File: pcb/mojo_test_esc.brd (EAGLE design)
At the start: 100 x 80 mm, 0 parts

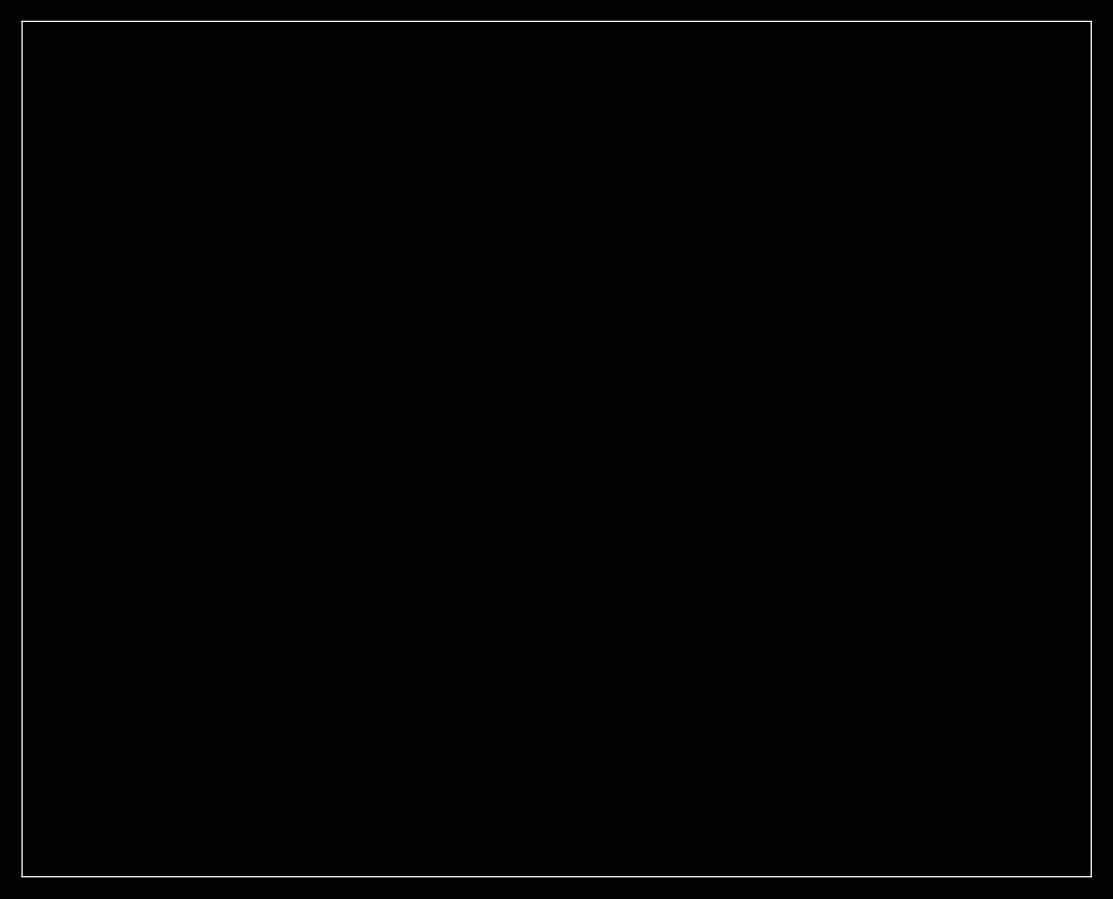
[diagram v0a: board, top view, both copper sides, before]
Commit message: Creating basic board layout/schematic from Mojo pinout
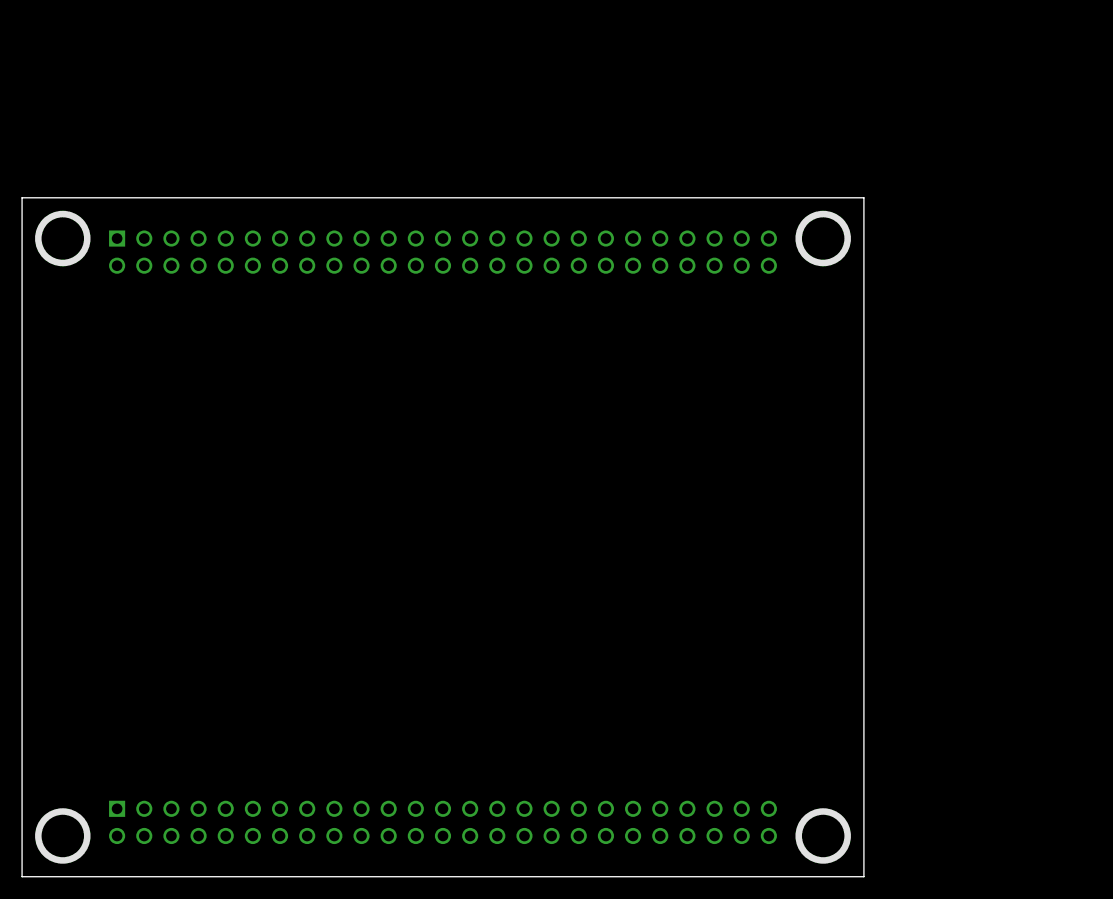
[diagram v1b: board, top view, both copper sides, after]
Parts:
- added B1: MOJO_NO_ANALOGV3_NO_LABEL, mojo_test_esc:MOJO_V3_NO_LABEL_NO_ANALOG
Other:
- board size 100 x 80 mm -> 78.7 x 63.5 mm
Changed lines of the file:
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@@
 <layer number="48" name="Document" color="7" fill="1" visible="yes" active="yes"/>
 <layer number="49" name="Reference" color="7" fill="1" visible="yes" active="yes"/>
+<layer number="50" name="dxf" color="7" fill="1" visible="no" active="no"/>
 <layer number="51" name="tDocu" color="7" fill="1" visible="yes" active="yes"/>
 <layer number="52" name="bDocu" color="7" fill="1" visible="yes" active="yes"/>
+<layer number="53" name="tGND_GNDA" color="7" fill="9" visible="no" active="no"/>
+<layer number="54" name="bGND_GNDA" color="1" fill="9" visible="no" active="no"/>
+<layer number="56" name="wert" color="7" fill="1" visible="no" active="no"/>
+<layer number="57" name="tCAD" color="7" fill="1" visible="no" active="no"/>
+<layer number="59" name="tCarbon" color="7" fill="1" visible="no" active="no"/>
+<layer number="60" name="bCarbon" color="7" fill="1" visible="no" active="no"/>
 <layer number="90" name="Modules" color="5" fill="1" visible="no" active="no"/>
 <layer number="91" name="Nets" color="2" fill="1" visible="no" active="no"/>
@@
 <layer number="97" name="Info" color="7" fill="1" visible="no" active="no"/>
 <layer number="98" name="Guide" color="6" fill="1" visible="no" active="no"/>
+<layer number="99" name="SpiceOrder" color="7" fill="1" visible="no" active="no"/>
+<layer number="100" name="Muster" color="7" fill="1" visible="no" active="no"/>
+<layer number="101" name="Patch_Top" color="12" fill="4" visible="yes" active="yes"/>
+<layer number="102" name="Vscore" color="7" fill="1" visible="yes" active="yes"/>
+<layer number="103" name="tMap" color="7" fill="1" visible="yes" active="yes"/>
+<layer number="104" name="Name" color="16" fill="1" visible="yes" active="yes"/>
+<layer number="105" name="tPlate" color="7" fill="1" visible="yes" active="yes"/>
+<layer number="106" name="bPlate" color="7" fill="1" visible="yes" active="yes"/>
+<layer number="107" name="Crop" color="7" fill="1" visible="yes" active="yes"/>
+<layer number="108" name="tplace-old" color="10" fill="1" visible="yes" active="yes"/>
+<layer number="109" name="ref-old" color="11" fill="1" visible="yes" active="yes"/>
+<layer number="110" name="fp0" color="7" fill="1" visible="yes" active="yes"/>
+<layer number="111" name="LPC17xx" color="7" fill="1" visible="yes" active="yes"/>
+<layer number="112" name="tSilk" color="7" fill="1" visible="yes" active="yes"/>
+<layer number="113" name="IDFDebug" color="7" fill="1" visible="yes" active="yes"/>
+<layer number="114" name="Badge_Outline" color="11" fill="1" visible="no" active="no"/>
+<layer number="115" name="ReferenceISLANDS" color="7" fill="1" visible="yes" active="yes"/>
+<layer number="116" name="Patch_BOT" color="9" fill="4" visible="yes" active="yes"/>
+<layer number="118" name="Rect_Pads" color="7" fill="1" visible="yes" active="yes"/>
+<layer number="121" name="_tsilk" color="7" fill="1" visible="yes" active="yes"/>
+<layer number="122" name="_bsilk" color="7" fill="1" visible="yes" active="yes"/>
+<layer number="123" name="tTestmark" color="7" fill="1" visible="yes" active="yes"/>
+<layer number="124" name="bTestmark" color="7" fill="1" visible="yes" active="yes"/>
+<layer number="125" name="_tNames" color="7" fill="1" visible="yes" active="yes"/>
+<layer number="126" name="_bNames" color="7" fill="1" visible="yes" active="yes"/>
+<layer number="127" name="_tValues" color="7" fill="1" visible="yes" active="yes"/>
+<layer number="128" name="_bValues" color="7" fill="1" visible="yes" active="yes"/>
+<layer number="129" name="Mask" color="7" fill="1" visible="yes" active="yes"/>
+<layer number="131" name="tAdjust" color="7" fill="1" visible="yes" active="yes"/>
+<layer number="132" name="bAdjust" color="7" fill="1" visible="yes" active="yes"/>
+<layer number="144" name="Drill_legend" color="7" fill="1" visible="yes" active="yes"/>
+<layer number="150" name="Notes" color="7" fill="1" visible="yes" active="yes"/>
+<layer number="151" name="HeatSink" color="7" fill="1" visible="yes" active="yes"/>
+<layer number="152" name="_bDocu" color="7" fill="1" visible="yes" active="yes"/>
+<layer number="153" name="FabDoc1" color="7" fill="1" visible="yes" active="yes"/>
+<layer number="154" name="FabDoc2" color="7" fill="1" visible="yes" active="yes"/>
+<layer number="155" name="FabDoc3" color="7" fill="1" visible="yes" active="yes"/>
+<layer number="199" name="Contour" color="7" fill="1" visible="yes" active="yes"/>
+<layer number="200" name="200bmp" color="1" fill="10" visible="yes" active="yes"/>
+<layer number="201" name="201bmp" color="2" fill="10" visible="yes" active="yes"/>
+<layer number="202" name="202bmp" color="3" fill="10" visible="yes" active="yes"/>
+<layer number="203" name="203bmp" color="4" fill="10" visible="yes" active="yes"/>
+<layer number="204" name="204bmp" color="5" fill="10" visible="yes" active="yes"/>
+<layer number="205" name="205bmp" color="6" fill="10" visible="yes" active="yes"/>
+<layer number="206" name="206bmp" color="7" fill="10" visible="yes" active="yes"/>
+<layer number="207" name="207bmp" color="8" fill="10" visible="yes" active="yes"/>
+<layer number="208" name="208bmp" color="9" fill="10" visible="yes" active="yes"/>
+<layer number="209" name="209bmp" color="7" fill="1" visible="yes" active="yes"/>
+<layer number="210" name="210bmp" color="7" fill="1" visible="yes" active="yes"/>
+<layer number="211" name="211bmp" color="7" fill="1" visible="yes" active="yes"/>
+<layer number="212" name="212bmp" color="7" fill="1" visible="yes" active="yes"/>
+<layer number="213" name="213bmp" color="7" fill="1" visible="yes" active="yes"/>
+<layer number="214" name="214bmp" color="7" fill="1" visible="yes" active="yes"/>
+<layer number="215" name="215bmp" color="7" fill="1" visible="yes" active="yes"/>
+<layer number="216" name="216bmp" color="7" fill="1" visible="yes" active="yes"/>
+<layer number="217" name="217bmp" color="18" fill="1" visible="no" active="no"/>
+<layer number="218" name="218bmp" color="19" fill="1" visible="no" active="no"/>
+<layer number="219" name="219bmp" color="20" fill="1" visible="no" active="no"/>
+<layer number="220" name="220bmp" color="21" fill="1" visible="no" active="no"/>
+<layer number="221" name="221bmp" color="22" fill="1" visible="no" active="no"/>
+<layer number="222" name="222bmp" color="23" fill="1" visible="no" active="no"/>
+<layer number="223" name="223bmp" color="24" fill="1" visible="no" active="no"/>
+<layer number="224" name="224bmp" color="25" fill="1" visible="no" active="no"/>
+<layer number="225" name="225bmp" color="7" fill="1" visible="yes" active="yes"/>
+<layer number="226" name="226bmp" color="7" fill="1" visible="yes" active="yes"/>
+<layer number="227" name="227bmp" color="7" fill="1" visible="yes" active="yes"/>
+<layer number="228" name="228bmp" color="7" fill="1" visible="yes" active="yes"/>
+<layer number="229" name="229bmp" color="7" fill="1" visible="yes" active="yes"/>
+<layer number="230" name="230bmp" color="7" fill="1" visible="yes" active="yes"/>
+<layer number="231" name="231bmp" color="7" fill="1" visible="yes" active="yes"/>
+<layer number="232" name="Eagle3D_PG2" color="7" fill="1" visible="yes" active="yes"/>
+<layer number="233" name="Eagle3D_PG3" color="7" fill="1" visible="yes" active="yes"/>
+<layer number="248" name="Housing" color="7" fill="1" visible="yes" active="yes"/>
+<layer number="249" name="Edge" color="7" fill="1" visible="yes" active="yes"/>
+<layer number="250" name="Descript" color="3" fill="1" visible="no" active="no"/>
+<layer number="251" name="SMDround" color="12" fill="11" visible="no" active="no"/>
+<layer number="254" name="cooling" color="7" fill="1" visible="yes" active="yes"/>
+<layer number="255" name="routoute" color="7" fill="1" visible="yes" active="yes"/>
 </layers>
 <board>
 <plain>
-<wire x1="0" y1="0" x2="100" y2="0" width="0" layer="20"/>
-<wire x1="100" y1="0" x2="100" y2="80" width="0" layer="20"/>
-<wire x1="100" y1="80" x2="0" y2="80" width="0" layer="20"/>
-<wire x1="0" y1="80" x2="0" y2="0" width="0" layer="20"/>
+<wire x1="0" y1="63.5" x2="78.74" y2="63.5" width="0" layer="20"/>
+<wire x1="78.74" y1="63.5" x2="78.74" y2="0" width="0" layer="20"/>
+<wire x1="78.74" y1="0" x2="0" y2="0" width="0" layer="20"/>
+<wire x1="0" y1="0" x2="0" y2="63.5" width="0" layer="20"/>
 </plain>
 <attributes>
@@
 </autorouter>
 <elements>
+<element name="B1" library="mojo_test_esc" package="MOJO_V3_NO_LABEL_NO_ANALOG" value="MOJO_NO_ANALOGV3_NO_LABEL" x="38.1" y="30.48"/>
 </elements>
 <signals>

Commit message: Adding D2PAK mosfet to library
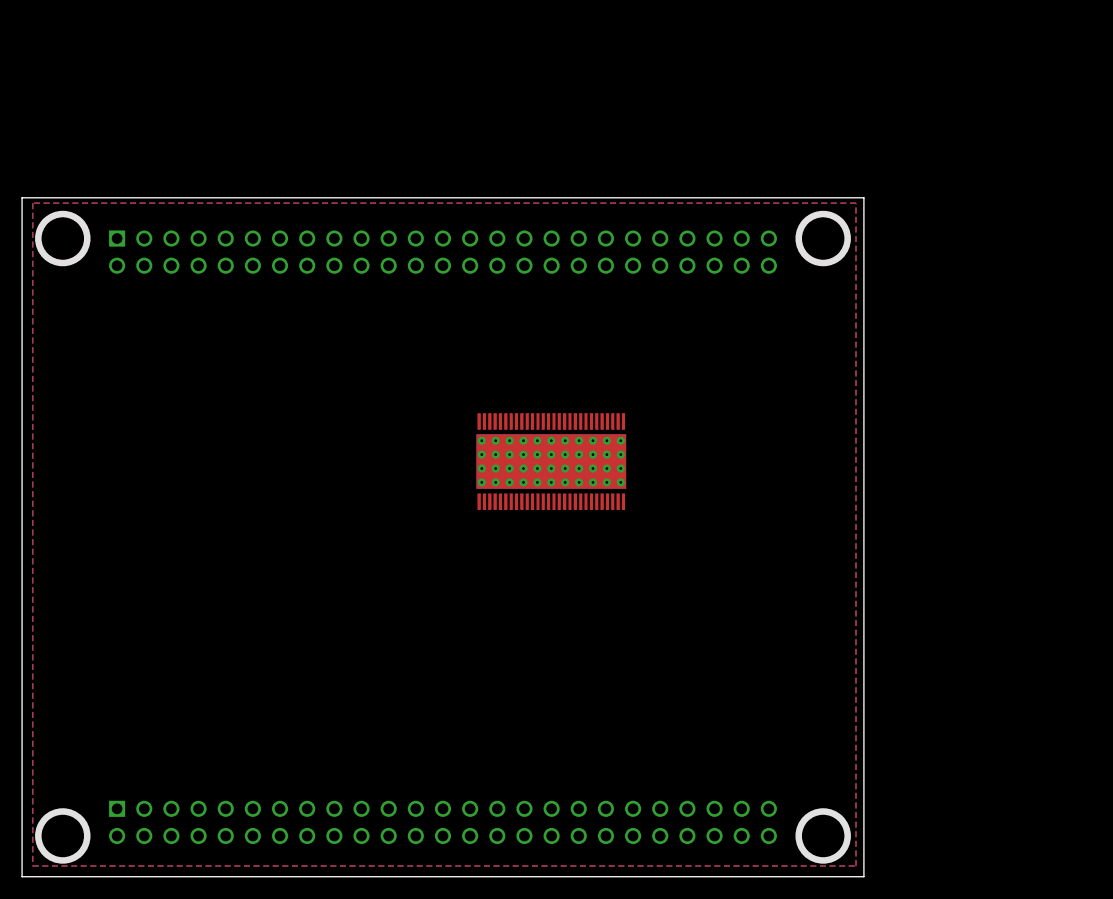
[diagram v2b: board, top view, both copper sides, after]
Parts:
- added U$1: DRV8302, mojo_test_esc:DRV8302
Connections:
- new net GND: U$1.GND_PAD, U$1.GND_PAD2, U$1.GND_PAD3, U$1.VIA1, U$1.VIA10, U$1.VIA11, U$1.VIA12, U$1.VIA13, U$1.VIA14, U$1.VIA15, U$1.VIA16, U$1.VIA17, U$1.VIA18, U$1.VIA19, U$1.VIA2, U$1.VIA20, U$1.VIA21, U$1.VIA22, U$1.VIA23, U$1.VIA24, U$1.VIA25, U$1.VIA26, U$1.VIA27, U$1.VIA28, U$1.VIA29, U$1.VIA3, U$1.VIA30, U$1.VIA31, U$1.VIA32, U$1.VIA33, U$1.VIA34, U$1.VIA35, U$1.VIA36, U$1.VIA37, U$1.VIA38, U$1.VIA39, U$1.VIA4, U$1.VIA40, U$1.VIA41, U$1.VIA42, U$1.VIA43, U$1.VIA44, U$1.VIA5, U$1.VIA6, U$1.VIA7, U$1.VIA8, U$1.VIA9
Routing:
- added copper zone on layer 1, net +12V
- added copper zone on layer 16, net GND
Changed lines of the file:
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@@
 <setting verticaltext="up"/>
 </settings>
-<grid distance="0.05" unitdist="inch" unit="inch" style="lines" multiple="1" display="no" altdistance="0.025" altunitdist="inch" altunit="inch"/>
+<grid distance="1" unitdist="mm" unit="mm" style="lines" multiple="1" display="yes" altdistance="0.025" altunitdist="inch" altunit="inch"/>
 <layers>
 <layer number="1" name="Top" color="4" fill="1" visible="yes" active="yes"/>
@@
 <layer number="27" name="tValues" color="7" fill="1" visible="yes" active="yes"/>
 <layer number="28" name="bValues" color="7" fill="1" visible="yes" active="yes"/>
-<layer number="29" name="tStop" color="7" fill="3" visible="no" active="yes"/>
-<layer number="30" name="bStop" color="7" fill="6" visible="no" active="yes"/>
-<layer number="31" name="tCream" color="7" fill="4" visible="no" active="yes"/>
-<layer number="32" name="bCream" color="7" fill="5" visible="no" active="yes"/>
-<layer number="33" name="tFinish" color="6" fill="3" visible="no" active="yes"/>
-<layer number="34" name="bFinish" color="6" fill="6" visible="no" active="yes"/>
-<layer number="35" name="tGlue" color="7" fill="4" visible="no" active="yes"/>
-<layer number="36" name="bGlue" color="7" fill="5" visible="no" active="yes"/>
-<layer number="37" name="tTest" color="7" fill="1" visible="no" active="yes"/>
-<layer number="38" name="bTest" color="7" fill="1" visible="no" active="yes"/>
+<layer number="29" name="tStop" color="7" fill="3" visible="yes" active="yes"/>
+<layer number="30" name="bStop" color="7" fill="6" visible="yes" active="yes"/>
+<layer number="31" name="tCream" color="7" fill="4" visible="yes" active="yes"/>
+<layer number="32" name="bCream" color="7" fill="5" visible="yes" active="yes"/>
+<layer number="33" name="tFinish" color="6" fill="3" visible="yes" active="yes"/>
+<layer number="34" name="bFinish" color="6" fill="6" visible="yes" active="yes"/>
+<layer number="35" name="tGlue" color="7" fill="4" visible="yes" active="yes"/>
+<layer number="36" name="bGlue" color="7" fill="5" visible="yes" active="yes"/>
+<layer number="37" name="tTest" color="7" fill="1" visible="yes" active="yes"/>
+<layer number="38" name="bTest" color="7" fill="1" visible="yes" active="yes"/>
 <layer number="39" name="tKeepout" color="4" fill="11" visible="yes" active="yes"/>
 <layer number="40" name="bKeepout" color="1" fill="11" visible="yes" active="yes"/>
@@
 <layer number="42" name="bRestrict" color="1" fill="10" visible="yes" active="yes"/>
 <layer number="43" name="vRestrict" color="2" fill="10" visible="yes" active="yes"/>
-<layer number="44" name="Drills" color="7" fill="1" visible="no" active="yes"/>
-<layer number="45" name="Holes" color="7" fill="1" visible="no" active="yes"/>
-<layer number="46" name="Milling" color="3" fill="1" visible="no" active="yes"/>
-<layer number="47" name="Measures" color="7" fill="1" visible="no" active="yes"/>
+<layer number="44" name="Drills" color="7" fill="1" visible="yes" active="yes"/>
+<layer number="45" name="Holes" color="7" fill="1" visible="yes" active="yes"/>
+<layer number="46" name="Milling" color="3" fill="1" visible="yes" active="yes"/>
+<layer number="47" name="Measures" color="7" fill="1" visible="yes" active="yes"/>
 <layer number="48" name="Document" color="7" fill="1" visible="yes" active="yes"/>
 <layer number="49" name="Reference" color="7" fill="1" visible="yes" active="yes"/>
@@
 <elements>
 <element name="B1" library="mojo_test_esc" package="MOJO_V3_NO_LABEL_NO_ANALOG" value="MOJO_NO_ANALOGV3_NO_LABEL" x="38.1" y="30.48"/>
+<element name="U$1" library="mojo_test_esc" package="DRV8302" value="DRV8302" x="49.5" y="38.83"/>
 </elements>
 <signals>
+<signal name="GND">
+<contactref element="U$1" pad="VIA30"/>
+<contactref element="U$1" pad="VIA4"/>
+<contactref element="U$1" pad="VIA9"/>
+<contactref element="U$1" pad="VIA42"/>
+<contactref element="U$1" pad="VIA21"/>
+<contactref element="U$1" pad="VIA5"/>
+<contactref element="U$1" pad="VIA10"/>
+<contactref element="U$1" pad="VIA3"/>
+<contactref element="U$1" pad="VIA15"/>
+<contactref element="U$1" pad="VIA27"/>
+<contactref element="U$1" pad="VIA7"/>
+<contactref element="U$1" pad="VIA1"/>
+<contactref element="U$1" pad="VIA18"/>
+<contactref element="U$1" pad="VIA13"/>
+<contactref element="U$1" pad="VIA11"/>
+<contactref element="U$1" pad="VIA22"/>
+<contactref element="U$1" pad="VIA35"/>
+<contactref element="U$1" pad="VIA36"/>
+<contactref element="U$1" pad="VIA14"/>
+<contactref element="U$1" pad="VIA38"/>
+<contactref element="U$1" pad="VIA28"/>
+<contactref element="U$1" pad="VIA6"/>
+<contactref element="U$1" pad="VIA26"/>
+<contactref element="U$1" pad="VIA2"/>
+<contactref element="U$1" pad="VIA19"/>
+<contactref element="U$1" pad="VIA32"/>
+<contactref element="U$1" pad="VIA33"/>
+<contactref element="U$1" pad="VIA25"/>
+<contactref element="U$1" pad="VIA24"/>
+<contactref element="U$1" pad="VIA23"/>
+<contactref element="U$1" pad="VIA12"/>
+<contactref element="U$1" pad="VIA41"/>
+<contactref element="U$1" pad="VIA40"/>
+<contactref element="U$1" pad="VIA43"/>
+<contactref element="U$1" pad="GND_PAD"/>
+<contactref element="U$1" pad="VIA29"/>
+<contactref element="U$1" pad="VIA17"/>
+<contactref element="U$1" pad="VIA37"/>
+<contactref element="U$1" pad="VIA16"/>
+<contactref element="U$1" pad="VIA20"/>
+<contactref element="U$1" pad="VIA8"/>
+<contactref element="U$1" pad="VIA39"/>
+<contactref element="U$1" pad="VIA31"/>
+<contactref element="U$1" pad="VIA34"/>
+<contactref element="U$1" pad="VIA44"/>
+<polygon width="0.4064" layer="16" isolate="0.381">
+<vertex x="1" y="1"/>
+<vertex x="78" y="1"/>
+<vertex x="78" y="62"/>
+<vertex x="78" y="63"/>
+<vertex x="1" y="63"/>
+</polygon>
+<contactref element="U$1" pad="GND_PAD2"/>
+<contactref element="U$1" pad="GND_PAD3"/>
+<wire x1="49.5" y1="38.83" x2="49.5" y2="38.83" width="0" layer="19" extent="1-16"/>
+</signal>
+<signal name="+12V">
+<polygon width="0.4064" layer="1" isolate="0.381">
+<vertex x="1" y="1"/>
+<vertex x="78" y="1"/>
+<vertex x="78" y="63"/>
+<vertex x="1" y="63"/>
+</polygon>
+</signal>
 </signals>
 </board>
